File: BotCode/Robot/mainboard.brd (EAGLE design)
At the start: 54 x 72.4 mm, 19 parts

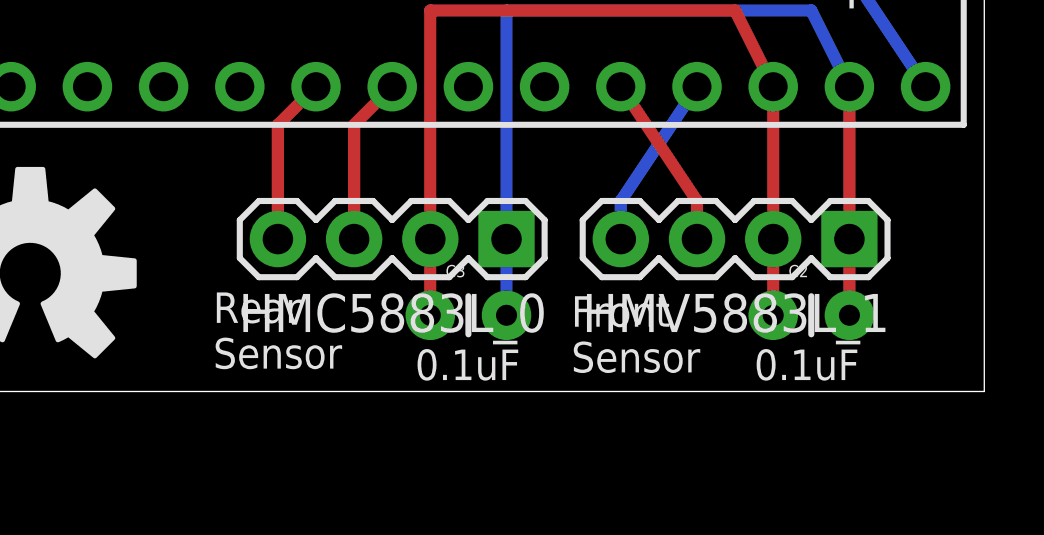
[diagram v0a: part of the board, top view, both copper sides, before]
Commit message: UI improvements
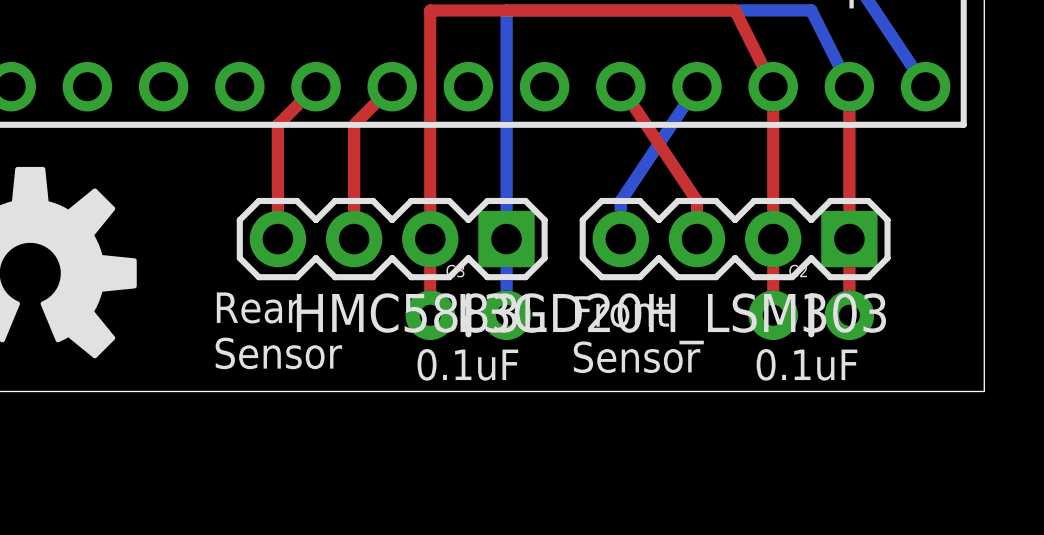
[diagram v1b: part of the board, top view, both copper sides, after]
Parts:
- renumbered HMC5883L_0 to HMC5883L, HMV5883L_1 to L3GD20H_LSM303
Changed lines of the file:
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@@
 <element name="C4" library="SparkFun-Passives" package="CPOL-RADIAL-100UF-25V" value="100 uF" x="12.7" y="41.91" rot="R180"/>
 <element name="FRAME1" library="SparkFun-Aesthetics" package="CREATIVE_COMMONS" value="FRAME-LETTER" x="-5.08" y="74.93"/>
-<element name="HMC5883L_0" library="SparkFun-Connectors" package="1X04" value="" x="38.1" y="5.08" rot="R180"/>
-<element name="HMV5883L_1" library="SparkFun-Connectors" package="1X04" value="" x="49.53" y="5.08" rot="R180"/>
+<element name="HMC5883L" library="SparkFun-Connectors" package="1X04" value="" x="38.1" y="5.08" rot="R180"/>
+<element name="L3GD20H_LSM303" library="SparkFun-Connectors" package="1X04" value="" x="49.53" y="5.08" rot="R180"/>
 <element name="LED_DRIVER" library="BillPorter" package="DIP-16" value="TLC5916/17DIP-16" x="40.64" y="59.69" rot="R270"/>
 <element name="L_SERVO" library="SparkFun-Electromechanical" package="1X03" value="SMALL_SERVO" x="3.81" y="31.75" rot="R90"/>
@@
 <contactref element="TEENSY_LC" pad="3.3V"/>
 <contactref element="TEENSY_LC" pad="3.3V1"/>
-<contactref element="HMV5883L_1" pad="2"/>
+<contactref element="L3GD20H_LSM303" pad="2"/>
 <contactref element="C2" pad="1"/>
-<contactref element="HMC5883L_0" pad="2"/>
+<contactref element="HMC5883L" pad="2"/>
 <contactref element="C3" pad="1"/>
 <wire x1="46.99" y1="10.16" x2="46.99" y2="5.08" width="0.4064" layer="1"/>
@@
 <signal name="N$16">
 <contactref element="TEENSY_LC" pad="18/A4"/>
-<contactref element="HMC5883L_0" pad="4"/>
+<contactref element="HMC5883L" pad="4"/>
 <wire x1="31.75" y1="10.16" x2="30.48" y2="8.89" width="0.4064" layer="1"/>
 <wire x1="30.48" y1="8.89" x2="30.48" y2="5.08" width="0.4064" layer="1"/>
 </signal>
 <signal name="N$17">
-<contactref element="HMC5883L_0" pad="3"/>
+<contactref element="HMC5883L" pad="3"/>
 <contactref element="TEENSY_LC" pad="19/A5"/>
 <wire x1="34.29" y1="10.16" x2="33.02" y2="8.89" width="0.4064" layer="1"/>
@@
 <signal name="N$20">
 <contactref element="TEENSY_LC" pad="23/A9"/>
-<contactref element="HMV5883L_1" pad="4"/>
+<contactref element="L3GD20H_LSM303" pad="4"/>
 <wire x1="44.45" y1="10.16" x2="41.91" y2="6.35" width="0.4064" layer="16"/>
 <wire x1="41.91" y1="6.35" x2="41.91" y2="5.08" width="0.4064" layer="16"/>
 </signal>
 <signal name="N$21">
-<contactref element="HMV5883L_1" pad="3"/>
+<contactref element="L3GD20H_LSM303" pad="3"/>
 <contactref element="TEENSY_LC" pad="22/A8"/>
 <wire x1="44.45" y1="6.35" x2="44.45" y2="5.08" width="0.4064" layer="1"/>
@@
 <signal name="AGND">
 <contactref element="TEENSY_LC" pad="AGND"/>
-<contactref element="HMV5883L_1" pad="1"/>
+<contactref element="L3GD20H_LSM303" pad="1"/>
 <contactref element="C2" pad="2"/>
-<contactref element="HMC5883L_0" pad="1"/>
+<contactref element="HMC5883L" pad="1"/>
 <contactref element="C3" pad="2"/>
 <wire x1="49.53" y1="10.16" x2="49.53" y2="5.08" width="0.4064" layer="1"/>

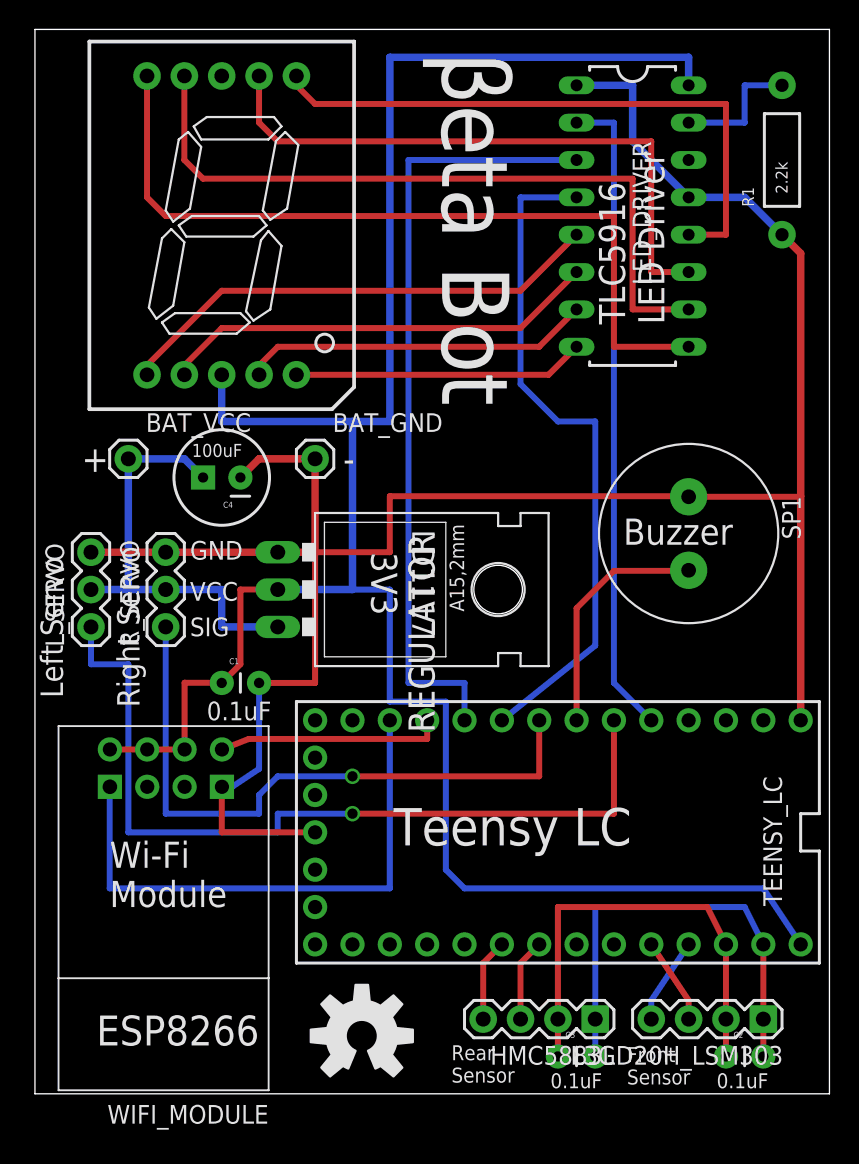
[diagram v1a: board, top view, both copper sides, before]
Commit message: Added initial support for robot tuning.
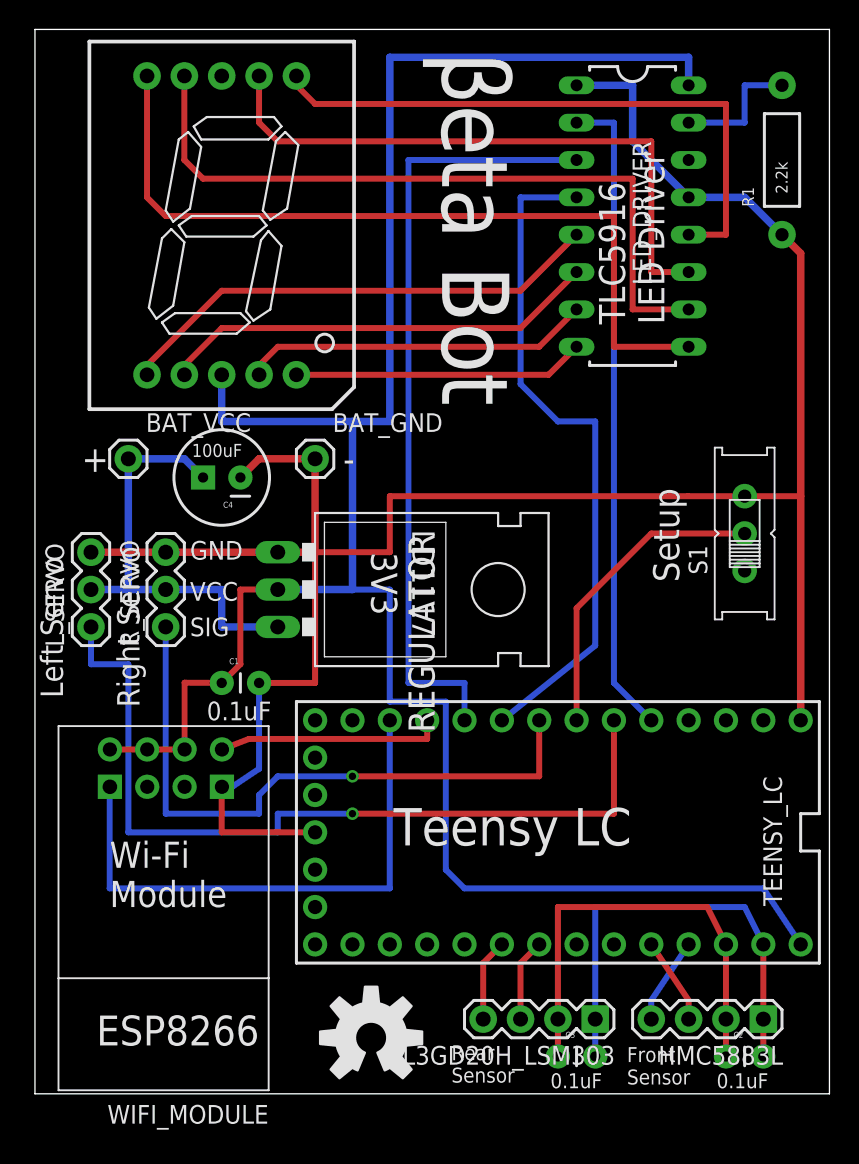
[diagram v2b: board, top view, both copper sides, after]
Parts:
- removed SP1: SPEAKER/PS12, adafruit:PS12
- removed U$5: (no value), SparkFun-Aesthetics:OSHW-LOGO-L
- added LOGO1: OSHW-LOGOL, SparkFun-Aesthetics:OSHW-LOGO-L
- added S1: Setup, adafruit:EG1218
- moved HMC5883L 11.4 mm to (49.5, 5.08)
- moved L3GD20H_LSM303 11.4 mm to (38.1, 5.08)
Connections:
- net N$1 renamed R_EXT
- net N$10 renamed LED_4
- net N$11 renamed LED_9
- net N$12 renamed LED_10
- net N$2 renamed SDI
- net N$3 renamed CLK
- net N$4 renamed LE
- net N$5 renamed LED_5
- net N$6 renamed LED_6
- net N$7 renamed LED_1
- net N$8 renamed LED_2
- net N$9 renamed LED_7
- removed net N$15: SP1.P$2, TEENSY_LC.5
- removed net N$16: HMC5883L.4, TEENSY_LC.18/A4
- removed net N$17: HMC5883L.3, TEENSY_LC.19/A5
- removed net N$20: L3GD20H_LSM303.4, TEENSY_LC.23/A9
- removed net N$21: L3GD20H_LSM303.3, TEENSY_LC.22/A8
- new net F_SCL: HMC5883L.3, TEENSY_LC.22/A8
- new net F_SDA: HMC5883L.4, TEENSY_LC.23/A9
- new net R_SCL: L3GD20H_LSM303.3, TEENSY_LC.19/A5
- new net R_SDA: L3GD20H_LSM303.4, TEENSY_LC.18/A4
- new net SETUP: S1.P, TEENSY_LC.5
- net GND: now also S1.S; no longer SP1.P$1
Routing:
- net SETUP: track 0.00 -> 21.2 mm
- net N$15: track 16.3 -> 0.00 mm
- net N$21: track 5.85 -> 0.00 mm
- net N$20: track 5.85 -> 0.00 mm
- net F_SDA: track 0.00 -> 5.85 mm
- net F_SCL: track 0.00 -> 5.85 mm
- net R_SDA: track 0.00 -> 5.61 mm
- net N$16: track 5.61 -> 0.00 mm
- net R_SCL: track 0.00 -> 5.61 mm
- net N$17: track 5.61 -> 0.00 mm
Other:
- board text added: "Setup"
- board text removed: "Buzzer"
